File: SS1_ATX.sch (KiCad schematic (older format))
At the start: 6 parts, among them J1 39299246, J2 15247140, U2 74LVC1G06

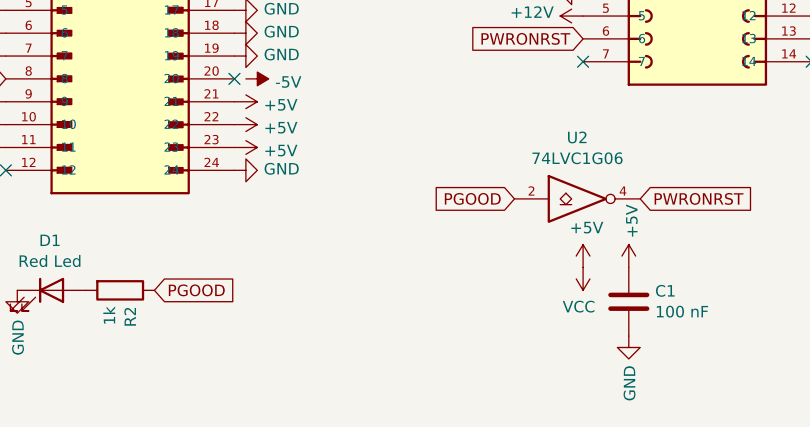
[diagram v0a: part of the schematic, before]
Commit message: oups, connect ~PS_ON to GND to turn on power
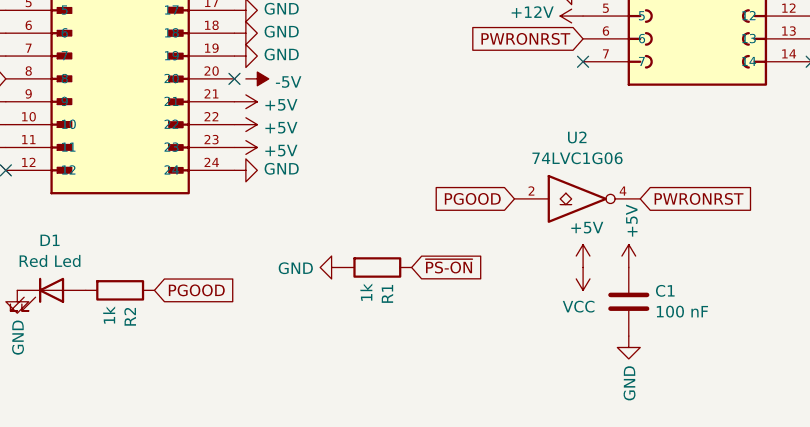
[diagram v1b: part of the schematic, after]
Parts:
- added R1: 1k, Resistor_SMD:R_0603_1608Metric, symbol Device:R
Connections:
- net GND: now also R1.2
- net ~PS-ON: now also R1.1
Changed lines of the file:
@@
 	-1   0    0    1
 $EndComp
+Text GLabel 5100 3750 2    50   Input ~ 0
+~PS-ON
+$Comp
+L power:GND #PWR0132
+U 1 1 644FB3A0
+P 4800 3750
+F 0 "#PWR0132" H 4800 3500 50  0001 C CNN
+F 1 "GND" V 4805 3622 50  0000 R CNN
+F 2 "" H 4800 3750 50  0001 C CNN
+F 3 "" H 4800 3750 50  0001 C CNN
+	1    4800 3750
+	0    1    1    0
+$EndComp
+$Comp
+L Device:R R1
+U 1 1 644FB63B
+P 4950 3750
+F 0 "R1" H 5020 3796 50  0000 L CNN
+F 1 "1k" H 5020 3705 50  0000 L CNN
+F 2 "Resistor_SMD:R_0603_1608Metric" V 4880 3750 50  0001 C CNN
+F 3 "~" H 4950 3750 50  0001 C CNN
+F 4 "0603WAF1001T5E" H 4950 3750 50  0001 C CNN "MPN"
+	1    4950 3750
+	0    1    1    0
+$EndComp
 $EndSCHEMATC

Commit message: more notes
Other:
- note added: "7, 14: excess pins, 2x6 doesnt seem to exist for PCB"
- note added: "From the SS2 service manual:\n« Note – The Por Signal is a TTL open collector and pull up is on the main logic board »\nand\n« Por is a Power-On reset TTL open collector signal \nfrom the power supply, which is activated after DC voltages have risen »"
- note removed: "From the SS2 service manual:\n« Note – The Por Signal is a TTL open collector and pull up is on the main logic board »"
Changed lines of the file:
@@
 EESchema Schematic File Version 4
-LIBS:SS1_ATX-cache
-EELAYER 26 0
+EELAYER 30 0
 EELAYER END
 $Descr A4 11693 8268
@@
 NoConn ~ 6850 2850
 NoConn ~ 5850 2850
-Text Notes 6850 2100 0    50   ~ 0
-From the SS2 service manual:\n« Note – The Por Signal is a TTL open collector and pull up is on the main logic board »
+Text Notes 6650 3700 0    50   ~ 0
+From the SS2 service manual:\n« Note – The Por Signal is a TTL open collector and pull up is on the main logic board »\nand\n« Por is a Power-On reset TTL open collector signal \nfrom the power supply, which is activated after DC voltages have risen »
 $Comp
 L 74xGxx:74LVC1G06 U2
@@
 	0    1    1    0
 $EndComp
+Text Notes 6900 2950 0    50   ~ 0
+7, 14: excess pins, 2x6 doesnt seem to exist for PCB
 $EndSCHEMATC

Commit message: upd, notes
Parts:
- J1, J2: DNP (none) -> DNP
- R1: value 1k -> 0; MPN 0603WAF1001T5E -> 0603WAF0000T5E
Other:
- note added: "No soft-power,\nso always on"
- note added: "https://shrubbery.net/~heas/sun-feh-2_1/Systems/Sun3/POWER_25_Sony-85.html"
